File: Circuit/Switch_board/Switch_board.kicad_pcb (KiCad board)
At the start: 2 copper layers, 40 x 31.7 mm, 31 parts, among them J1 switch_mode, J2 switch, M3 MountingHole_3mm, P1 XT30, Q1 2N7002, Q2 2N7002, Q3 2N7002, Q4 2N7002, U1 DRV5023

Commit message: corrected silkskins that descript each LEDs and adjusted NO. and Note to middle of Switch_board PCB
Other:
- board text added: "NO._________Note______________________________"
- board text removed: "NO.________ Note______________________________"
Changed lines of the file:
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@@
     (arrow2b (pts (xy 179.705 143.891) (xy 178.578496 144.477421)))
   )
-  (gr_text "NO.________ Note______________________________" (at 160.782 129.667) (layer B.SilkS)
+  (gr_text NO._________Note______________________________ (at 159.766 129.667) (layer B.SilkS)
     (effects (font (size 1 1) (thickness 0.25)) (justify mirror))
   )
@@
     (effects (font (size 1 1) (thickness 0.25)))
   )
-  (gr_text "IS SWITCH HIGH" (at 158.75 113.665 90) (layer B.SilkS)
+  (gr_text "IS SWITCH HIGH" (at 162.052 113.665 90) (layer B.SilkS)
     (effects (font (size 0.7 0.7) (thickness 0.175)) (justify mirror))
   )
-  (gr_text "HALL SENSOR OUT" (at 154.94 114.3 90) (layer B.SilkS)
+  (gr_text "HALL SENSOR OUT" (at 158.877 114.3254 90) (layer B.SilkS)
     (effects (font (size 0.7 0.7) (thickness 0.175)) (justify mirror))
   )
-  (gr_text PWR (at 162.052 110.617 90) (layer B.SilkS)
+  (gr_text PWR (at 155.321 110.617 90) (layer B.SilkS)
     (effects (font (size 0.7 0.7) (thickness 0.175)) (justify mirror))
   )

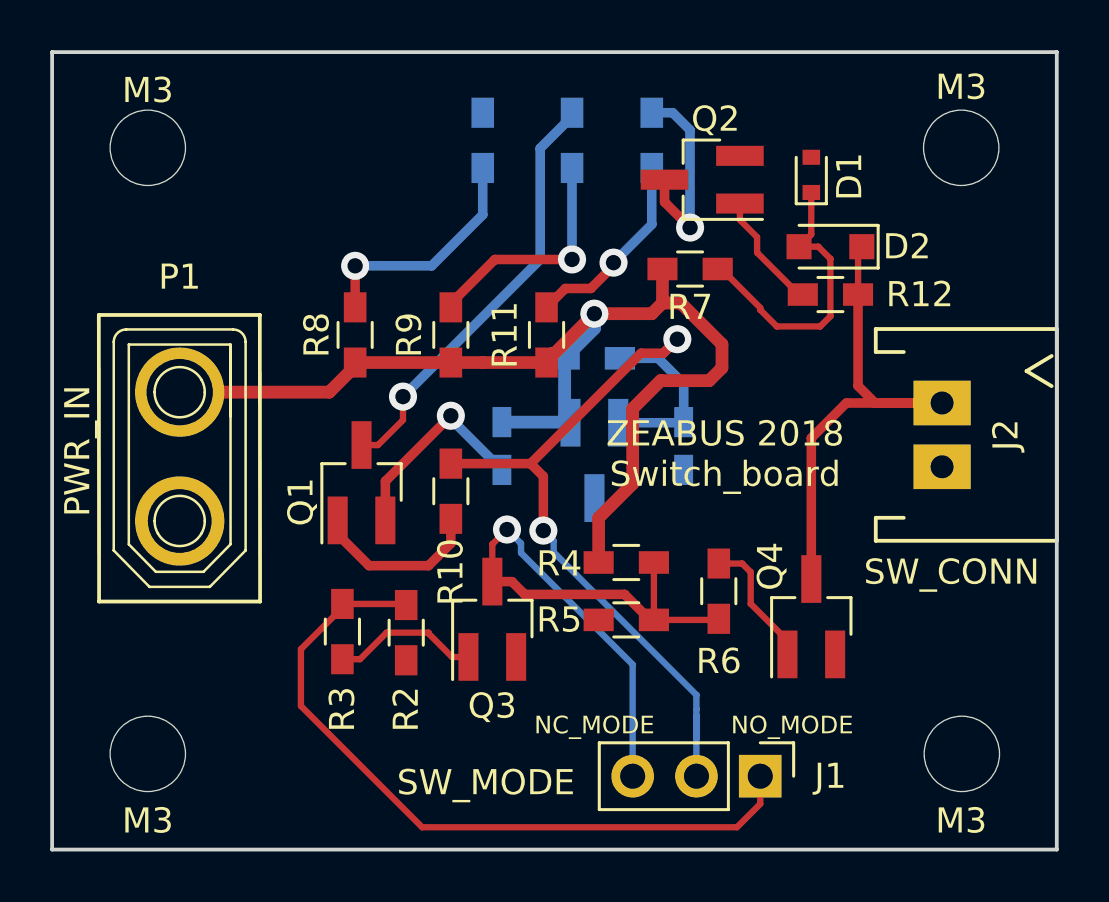
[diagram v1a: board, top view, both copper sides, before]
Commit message: moved hall sensor and LEDs to middle of PCB on Switch_board
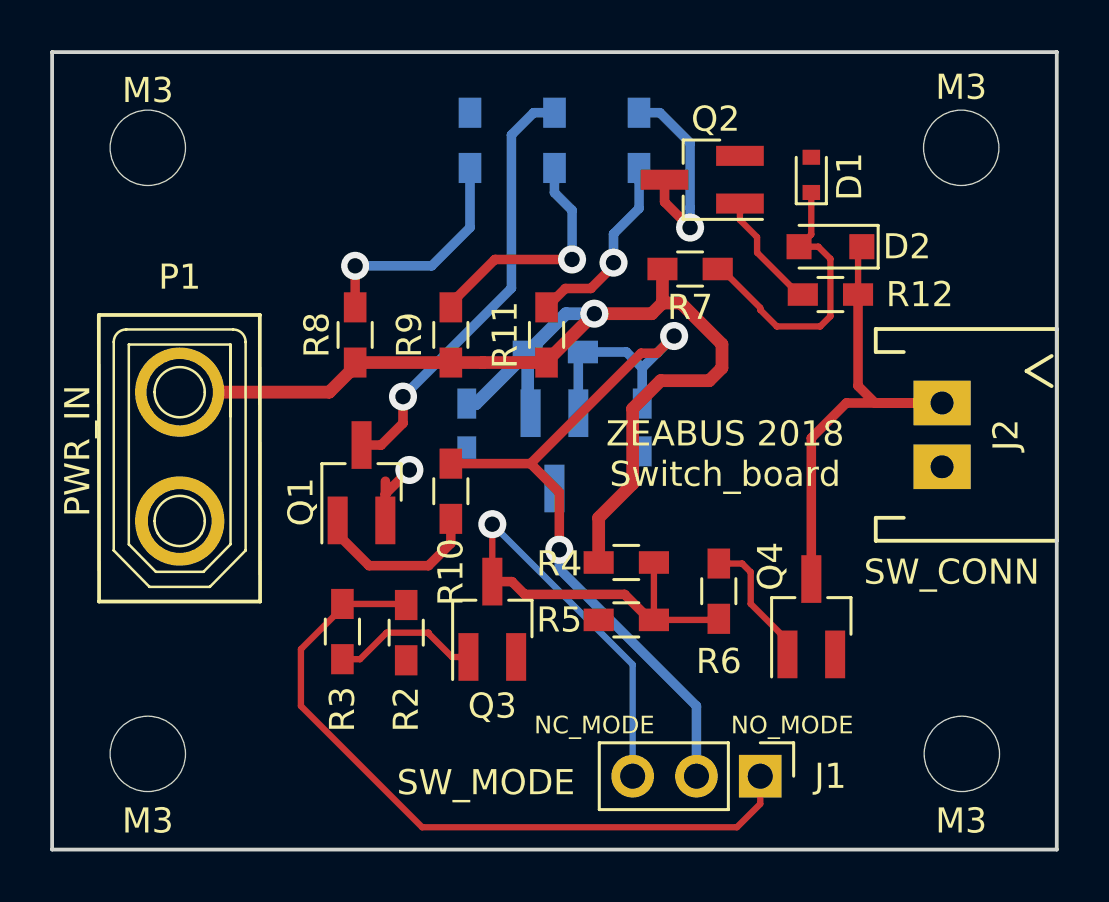
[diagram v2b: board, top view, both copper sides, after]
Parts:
- moved C2 1.81 mm to (163.2, 122.9)
- moved U1 1.64 mm to (159.7, 123.8)
- moved C1 1.58 mm to (156.2, 122.9)
- moved R1 1.49 mm to (159.7, 119.9)
- moved D4 0.70 mm to (159.7, 111.5)
- moved D3 0.51 mm to (156.3, 111.5)
- moved D5 0.51 mm to (163.1, 111.5)
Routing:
- net GND: track 8.24 -> 3.96 mm
- net VCC: track 44.7 -> 46.1 mm
- net hall_sensor_out: track 35.3 -> 34.5 mm

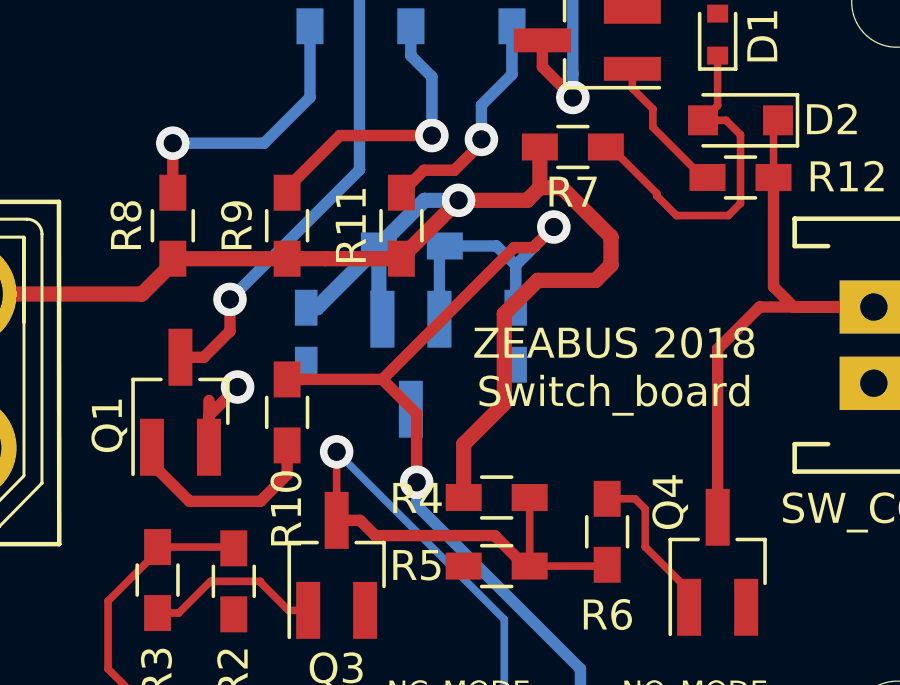
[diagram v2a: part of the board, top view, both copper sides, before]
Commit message: moved out components opposite side of hall sensor on Switch_board
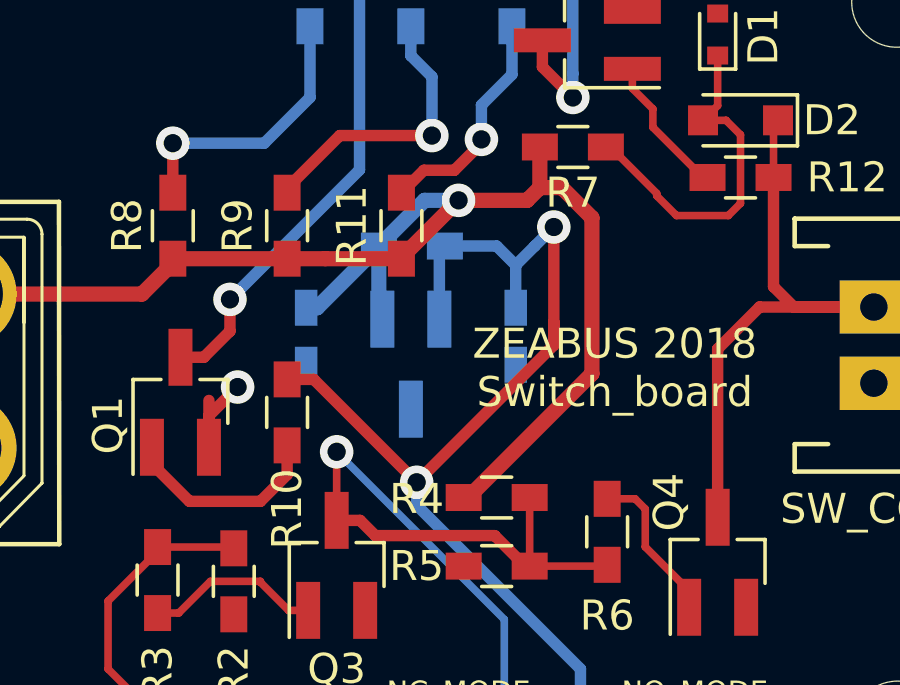
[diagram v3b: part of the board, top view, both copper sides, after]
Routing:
- net hall_sensor_out: track 34.5 -> 36.3 mm
- net VCC: track 46.1 -> 44.5 mm
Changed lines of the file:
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@@
     (thickness 1.6)
     (drawings 17)
-    (tracks 153)
+    (tracks 149)
     (zones 0)
     (modules 31)
@@
   (gr_line (start 179.705 107.95) (end 139.7 107.95) (layer Edge.Cuts) (width 0.15))
   (gr_line (start 179.7 139.7) (end 179.7 107.95) (layer Edge.Cuts) (width 0.15))
+  (segment (start 161.46 128.27) (end 161.61 128.27) (width 0.508) (layer F.Cu) (net 1))
+  (segment (start 161.61 128.27) (end 165.735 124.145) (width 0.508) (layer F.Cu) (net 1))
+  (segment (start 164.730866 117.94) (end 164 117.94) (width 0.508) (layer F.Cu) (net 1))
+  (segment (start 165.735 124.145) (end 165.735 118.944134) (width 0.508) (layer F.Cu) (net 1))
+  (segment (start 165.735 118.944134) (end 164.730866 117.94) (width 0.508) (layer F.Cu) (net 1))
   (segment (start 156.21 121.9454) (end 156.5754 121.9454) (width 0.508) (layer B.Cu) (net 1))
   (segment (start 156.5754 121.9454) (end 158.6328 119.888) (width 0.508) (layer B.Cu) (net 1))
@@
   (segment (start 161.29 118.364) (end 160.1568 118.364) (width 0.508) (layer B.Cu) (net 1))
   (segment (start 160.1568 118.364) (end 158.6328 119.888) (width 0.508) (layer B.Cu) (net 1))
-  (segment (start 166.37 120.523) (end 166.37 119.579134) (width 0.508) (layer F.Cu) (net 1))
-  (segment (start 166.37 119.579134) (end 164.730866 117.94) (width 0.508) (layer F.Cu) (net 1))
-  (segment (start 164.730866 117.94) (end 164 117.94) (width 0.508) (layer F.Cu) (net 1))
-  (segment (start 165.862 121.031) (end 166.37 120.523) (width 0.508) (layer F.Cu) (net 1))
-  (segment (start 163.928842 121.031) (end 165.862 121.031) (width 0.508) (layer F.Cu) (net 1))
-  (segment (start 162.814 125.138) (end 162.814 122.145842) (width 0.508) (layer F.Cu) (net 1))
-  (segment (start 162.814 122.145842) (end 163.928842 121.031) (width 0.508) (layer F.Cu) (net 1))
   (segment (start 163.576 118.364) (end 164 117.94) (width 0.508) (layer F.Cu) (net 1))
   (segment (start 164 117.94) (end 164 116.586) (width 0.508) (layer F.Cu) (net 1))
@@
   (segment (start 159.385 120.269) (end 161.29 118.364) (width 0.508) (layer F.Cu) (net 1))
   (via (at 161.29 118.364) (size 1.1176) (drill 0.6096) (layers F.Cu B.Cu) (net 1))
-  (segment (start 161.46 126.492) (end 161.46 128.27) (width 0.508) (layer F.Cu) (net 1))
-  (segment (start 162.814 125.138) (end 161.46 126.492) (width 0.508) (layer F.Cu) (net 1))
   (segment (start 156.845 120.31) (end 159.385 120.31) (width 0.508) (layer F.Cu) (net 1))
   (segment (start 155.575 120.31) (end 156.845 120.31) (width 0.508) (layer F.Cu) (net 1))
@@
   (segment (start 167.767 115.317) (end 167.084 114.634) (width 0.254) (layer F.Cu) (net 7))
   (segment (start 167.084 114.634) (end 167.084 113.98) (width 0.254) (layer F.Cu) (net 7))
-  (segment (start 158.75 124.333) (end 159.893 125.476) (width 0.381) (layer F.Cu) (net 8))
-  (segment (start 159.893 125.476) (end 159.893 127.762) (width 0.381) (layer F.Cu) (net 8))
+  (segment (start 164.465 122.936) (end 164.465 122.428) (width 0.381) (layer F.Cu) (net 8))
+  (segment (start 164.465 122.428) (end 164.465 119.253) (width 0.381) (layer F.Cu) (net 8))
+  (segment (start 159.893 127.762) (end 164.465 123.19) (width 0.381) (layer F.Cu) (net 8))
+  (segment (start 164.465 123.19) (end 164.465 122.428) (width 0.381) (layer F.Cu) (net 8))
+  (segment (start 155.575 124.333) (end 156.464 124.333) (width 0.381) (layer F.Cu) (net 8))
+  (segment (start 156.464 124.333) (end 159.893 127.762) (width 0.381) (layer F.Cu) (net 8))
   (segment (start 159.893 128.524) (end 165.354 133.985) (width 0.381) (layer B.Cu) (net 8))
   (segment (start 165.354 133.985) (end 165.354 136.779) (width 0.381) (layer B.Cu) (net 8))
   (segment (start 159.893 127.762) (end 159.893 128.524) (width 0.381) (layer B.Cu) (net 8))
-  (segment (start 155.575 124.333) (end 158.75 124.333) (width 0.381) (layer F.Cu) (net 8))
-  (segment (start 163.144201 119.938799) (end 163.779201 119.938799) (width 0.381) (layer F.Cu) (net 8))
-  (segment (start 163.779201 119.938799) (end 164.465 119.253) (width 0.381) (layer F.Cu) (net 8))
   (segment (start 163.83 119.888) (end 164.465 119.253) (width 0.381) (layer B.Cu) (net 8))
   (segment (start 163.195 120.523) (end 163.83 119.888) (width 0.381) (layer B.Cu) (net 8))
@@
   (segment (start 160.65 120.0708) (end 160.8328 119.888) (width 0.381) (layer B.Cu) (net 8))
   (via (at 159.893 127.762) (size 1.1176) (drill 0.6096) (layers F.Cu B.Cu) (net 8))
-  (segment (start 163.144201 119.938799) (end 158.75 124.333) (width 0.381) (layer F.Cu) (net 8))
   (via (at 164.465 119.253) (size 1.1176) (drill 0.6096) (layers F.Cu B.Cu) (net 8))
   (segment (start 169.926 128.929) (end 169.926 123.317) (width 0.381) (layer F.Cu) (net 9))
